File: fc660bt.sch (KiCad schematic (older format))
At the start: 47 parts, among them J1 USB_B_Mini, J10 SWDIO, J11 FCTRYRST, J12 DFU, J13 VCC, J14 VBAT, J2 Conn_01x20, J3 Conn_01x02, J4 ICSP, J5 GND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

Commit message: Cleaned up and added comments to schematic
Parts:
- removed R8: 1K, Resistor_SMD:R_0805_2012Metric, symbol Device:R_Small
- H1, H2: symbol Mechanical:MountingHole -> Mechanical:MountingHole_Pad
- J3: value Conn_01x02 -> JST_PH
- J7: value +5v -> 5V
- J8: value +3.3v -> 3.3V
- R1, R2: symbol Device:R_Small -> Device:R
- SW1: value SW_Push -> RESET
- Y1: value Resonator -> 8MHz
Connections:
- net FG: now also H1.1, H2.1
- net GND: now also U1.33 (~HWB~/PE2)
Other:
- note added: "Battery charging circuit"
- note added: "For disconnecting MDBT40 if SWD\nprogramming 32u4 with 5V GPIO"
- note added: "Interface to fc660c keyboard pcb\nSee https://geekhack.org/index.php?topic=88439"
- note added: "SPI Bluetooth module\nSee https://learn.adafruit.com/adafruit-feather-32u4-bluefruit-le/downloads"
- note added: "SWD Programming breakout"
- note removed: "Battery circuit"
- moved on the sheet: C10, C3, C5, C6, C7, C8, D2, H3, H4, J1, J10, J11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

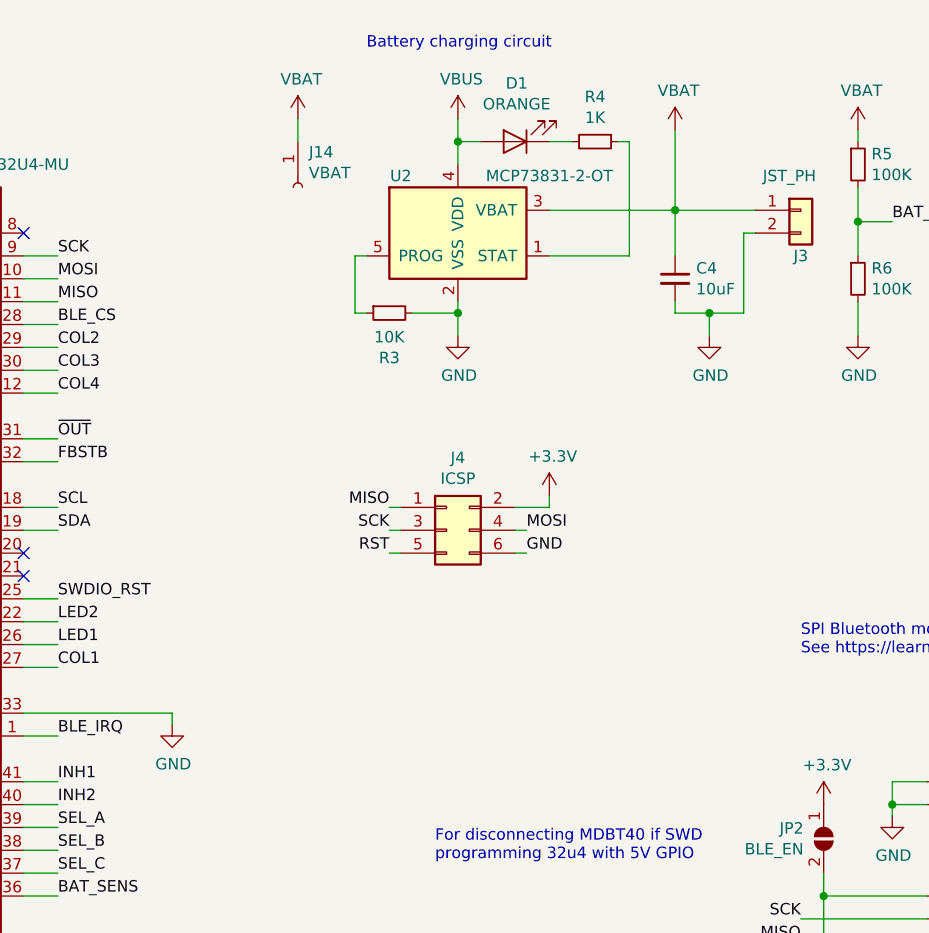
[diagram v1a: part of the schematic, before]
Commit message: Added switch to connect and disconnect battery
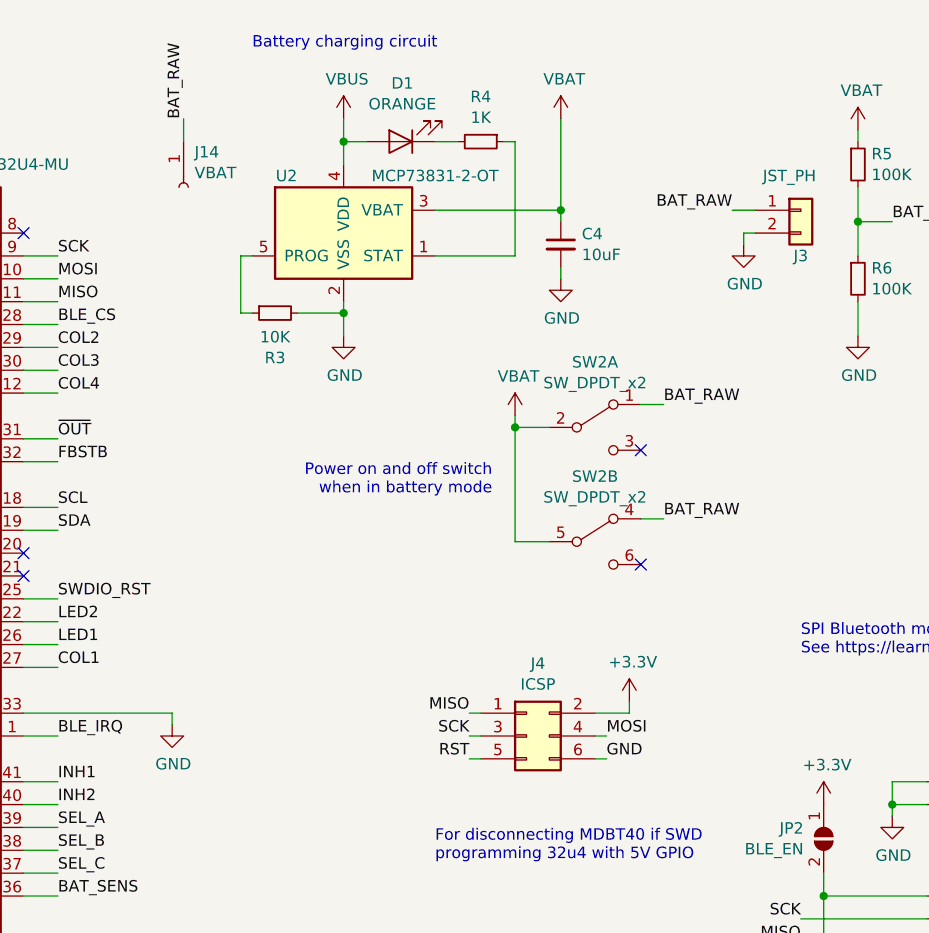
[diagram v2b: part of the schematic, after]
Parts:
- added SW2: SW_DPDT_x2, fc660bt:JS202011CQN, symbol Switch:SW_DPDT_x2
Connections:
- net VBAT: now also SW2.2 (B), SW2.5 (B); no longer J14.1 (Pin_1), J3.1 (Pin_1)
- new net BAT_RAW: J14.1 (Pin_1), J3.1 (Pin_1), SW2.1 (A), SW2.4 (A)
- no-connect marks 28 -> 30
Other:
- note added: "Power on and off switch\nwhen in battery mode"
- moved on the sheet: C4, D1, J14, J4, R3, R4, U2
